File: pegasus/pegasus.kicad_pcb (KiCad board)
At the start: 2 copper layers, 50 x 120 mm, 15 parts, among them IC1 RFD900, IC2 Adafruit_MPL3115A2, IC3 Adafruit-BNO055-PCB, IC4 L70B-M39, IC5 L7805ACV, J1 Conn_01x02_Female, J2 Conn_01x02_Female, U1 Teensy4.1, U2 CON-SMA-EDGE-S, U3 CON-SMA-EDGE-S

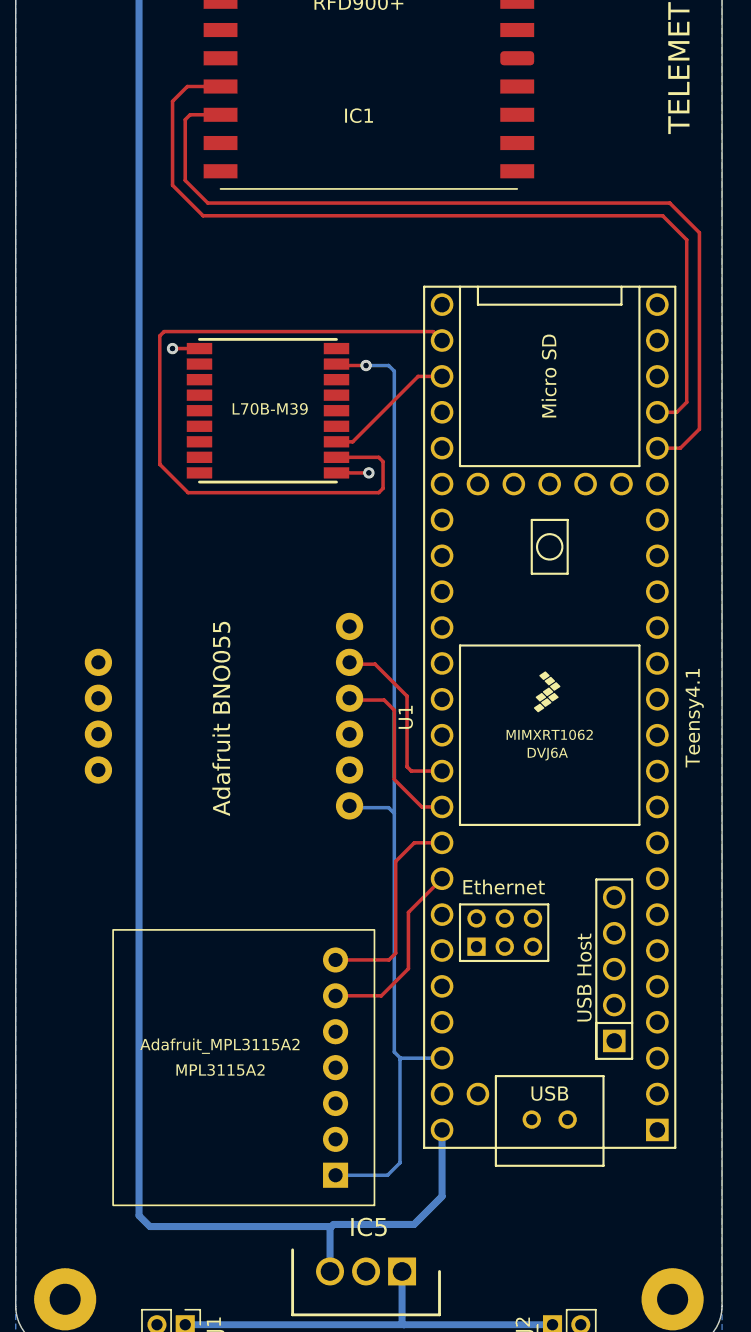
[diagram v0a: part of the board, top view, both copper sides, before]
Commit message: replace teensy 4.1 wih teensy 4, remove barometer and IMU
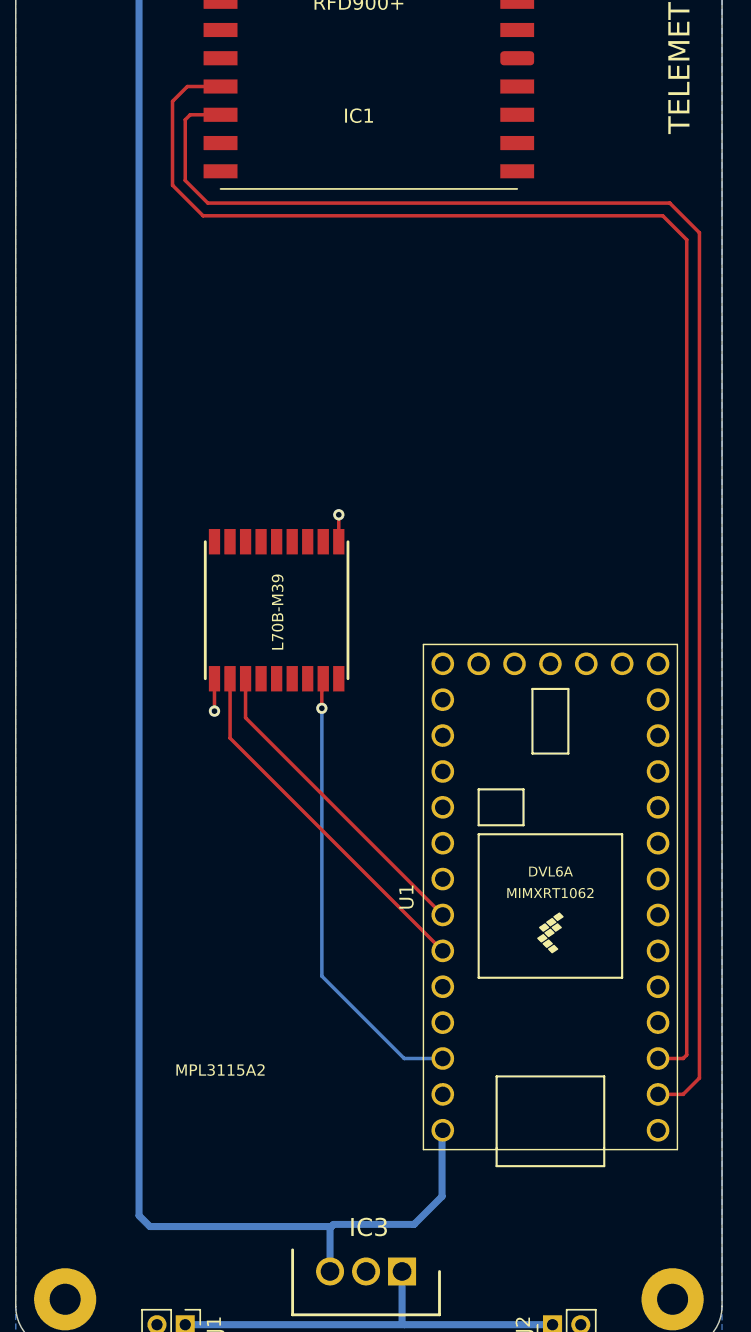
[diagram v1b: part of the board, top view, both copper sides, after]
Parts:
- removed the IC2 at (100.1, 140.1)
- removed the IC3 at (94.6, 115.3)
- IC3: renamed from IC5; footprint Voltage Regulator:TO255P460X1020X2008-3P -> SamaSys:TO255P460X1020X2008-3P
- U1: value Teensy4.1 -> Teensy4.0; footprint Teensy_4.1:Teensy_4.1 -> Teensy:Teensy40
- moved IC2 14.1 mm to (98.5, 107.7), turned to 90 degrees
- moved U1 12.7 mm to (117.8, 128.0)
- renumbered IC4 to IC2
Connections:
- IC2 pad 8: /+3.3V -> 3.3V
- U1 pad 2: unconnected-(U1-Pad2) -> RX7
- U1 pad 20: RX7 -> unconnected-(U1-Pad20)
- U1 pad 21: TX7 -> unconnected-(U1-Pad21)
- U1 pad 26: RX8 -> unconnected-(U1-Pad26)
- U1 pad 28: unconnected-(U1-Pad28) -> RX8
- U1 pad 3: unconnected-(U1-Pad3) -> TX7
- U1 pad 31: unconnected-(U1-Pad31) -> 3.3V
- U1 pad 32: unconnected-(U1-Pad32) -> GND
- U1 pad 33: unconnected-(U1-Pad33) -> +5V
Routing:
- net /+3.3V: track 71.4 -> 0.00 mm, vias 1 -> 0
- net TX7: track 61.6 -> 107.6 mm
- net RX7: track 62.3 -> 108.1 mm
- net 3.3V: track 0.00 -> 32.1 mm, vias 0 -> 1
- net RX8: track 51.5 -> 25.5 mm
- net /SDA: track 14.8 -> 0.00 mm
- net /SCL: track 13.3 -> 0.00 mm
- net TX8: track 9.39 -> 22.5 mm
- net /SCL1: track 12.2 -> 0.00 mm
- net /SDA1: track 12.2 -> 0.00 mm

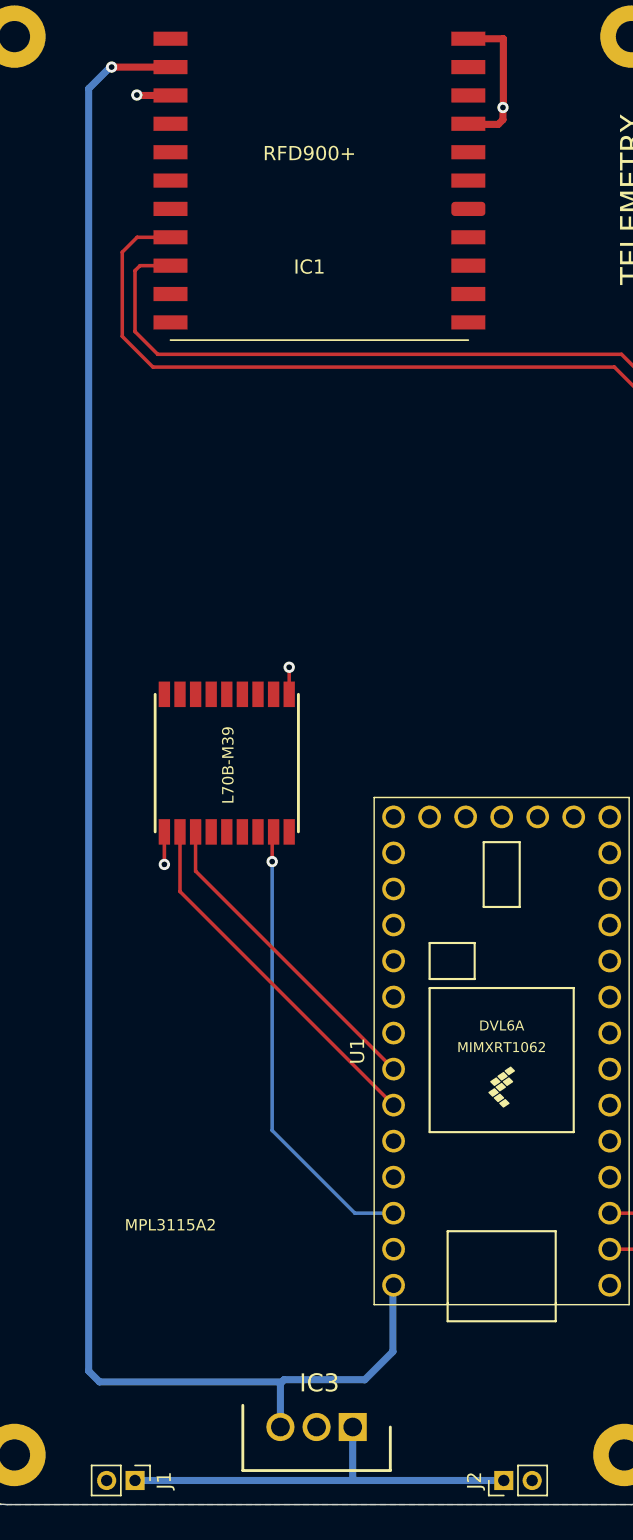
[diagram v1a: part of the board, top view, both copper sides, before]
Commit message: replace sma-connectors with screw terminal with switch
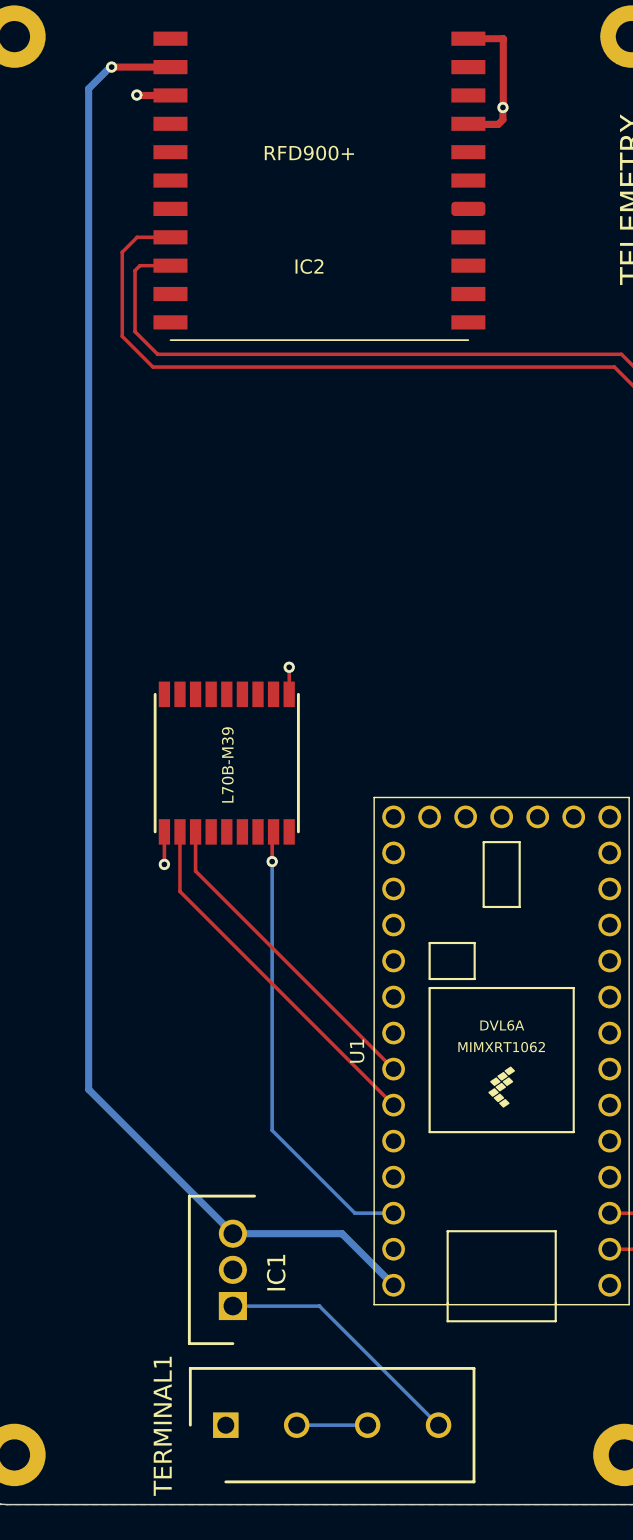
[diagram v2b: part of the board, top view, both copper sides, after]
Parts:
- removed J1, J2: Conn_01x02_Female, Connector_PinHeader_2.00mm:PinHeader_1x02_P2.00mm_Vertical
- added TERMINAL1: Screw_Terminal_01x04, RS-Components:SHDR4W100P0X500_1X4_2000X800X1000P, F.Cu at (98.4, 154.4)
- IC1: renamed from IC3; footprint SamaSys:TO255P460X1020X2008-3P -> RS-Components:TO255P460X1020X2008-3P
- moved IC1 12.0 mm to (98.9, 146.0), turned to 90 degrees
- renumbered IC1 to IC2, IC2 to IC3
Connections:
- IC1 pad 1: +3.7V -> /BATT+
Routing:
- net +3.7V: track 29.8 -> 0.00 mm
- net +5V: track 127.5 -> 104.1 mm
- net /BATT+: track 0.00 -> 18.0 mm
- net Net-(TERMINAL1-Pad2): track 0.00 -> 5.00 mm
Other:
- board text removed: "MPL3115A2"

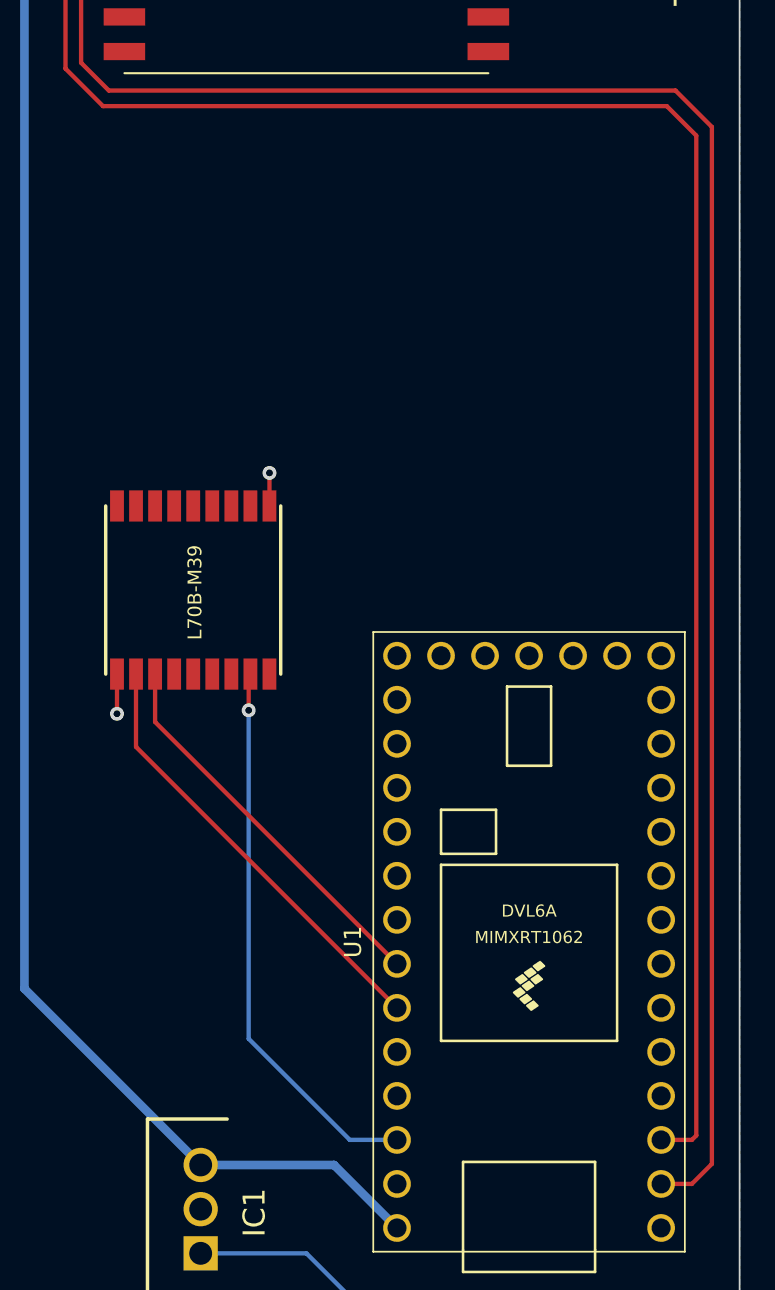
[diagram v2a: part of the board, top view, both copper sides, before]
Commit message: add external RX TX connectors
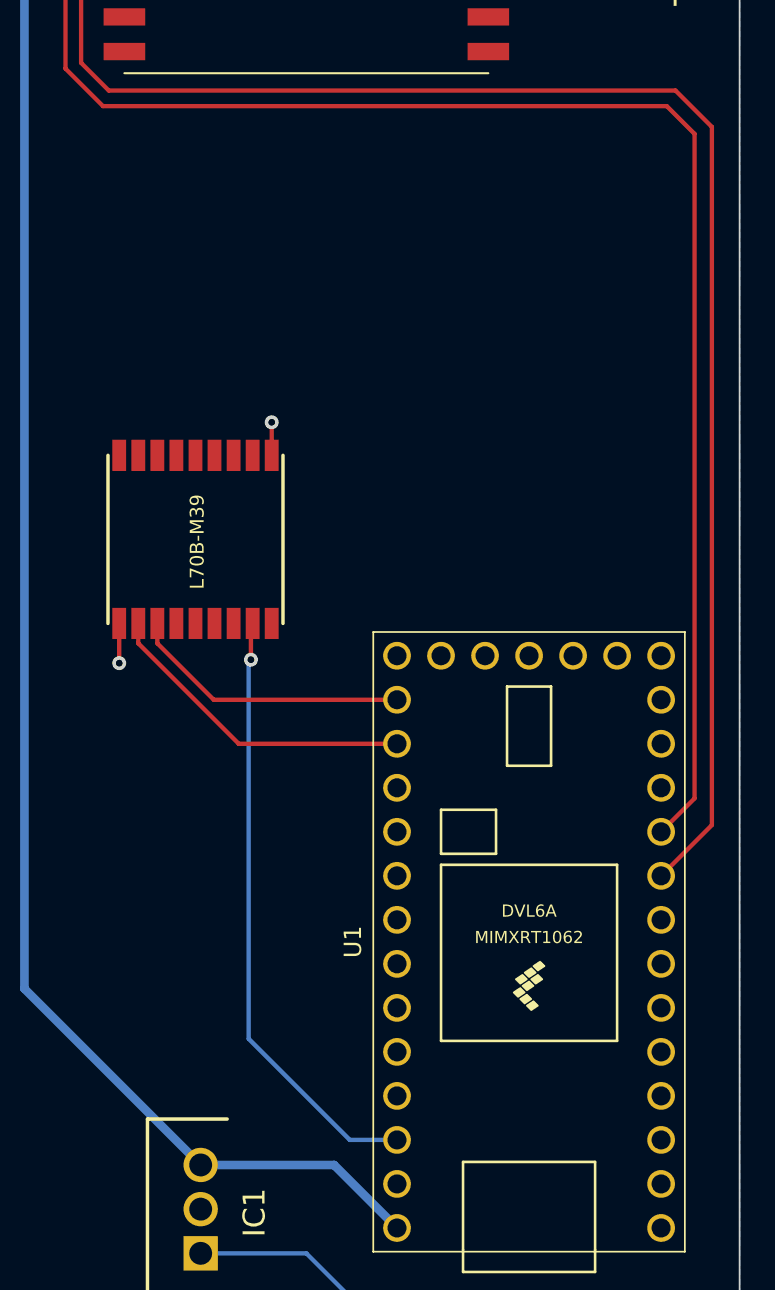
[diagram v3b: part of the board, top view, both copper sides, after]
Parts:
- moved IC3 2.92 mm to (98.6, 104.8)
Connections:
- IC3 pad 2: RX8 -> RX3
- IC3 pad 3: TX8 -> TX3
- U1 pad 10: unconnected-(U1-Pad10) -> TX7
- U1 pad 2: RX7 -> unconnected-(U1-Pad2)
- U1 pad 21: unconnected-(U1-Pad21) -> TX3
- U1 pad 22: unconnected-(U1-Pad22) -> RX3
- U1 pad 27: TX8 -> unconnected-(U1-Pad27)
- U1 pad 28: RX8 -> unconnected-(U1-Pad28)
- U1 pad 3: TX7 -> unconnected-(U1-Pad3)
- U1 pad 9: unconnected-(U1-Pad9) -> RX7
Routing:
- net RX8: track 25.5 -> 0.00 mm
- net TX8: track 22.5 -> 0.00 mm
- net TX7: track 107.6 -> 88.7 mm
- net RX7: track 108.1 -> 89.3 mm
- net RX3: track 0.00 -> 18.5 mm
- net TX3: track 0.00 -> 16.3 mm
- net 3.3V: track 32.1 -> 35.0 mm

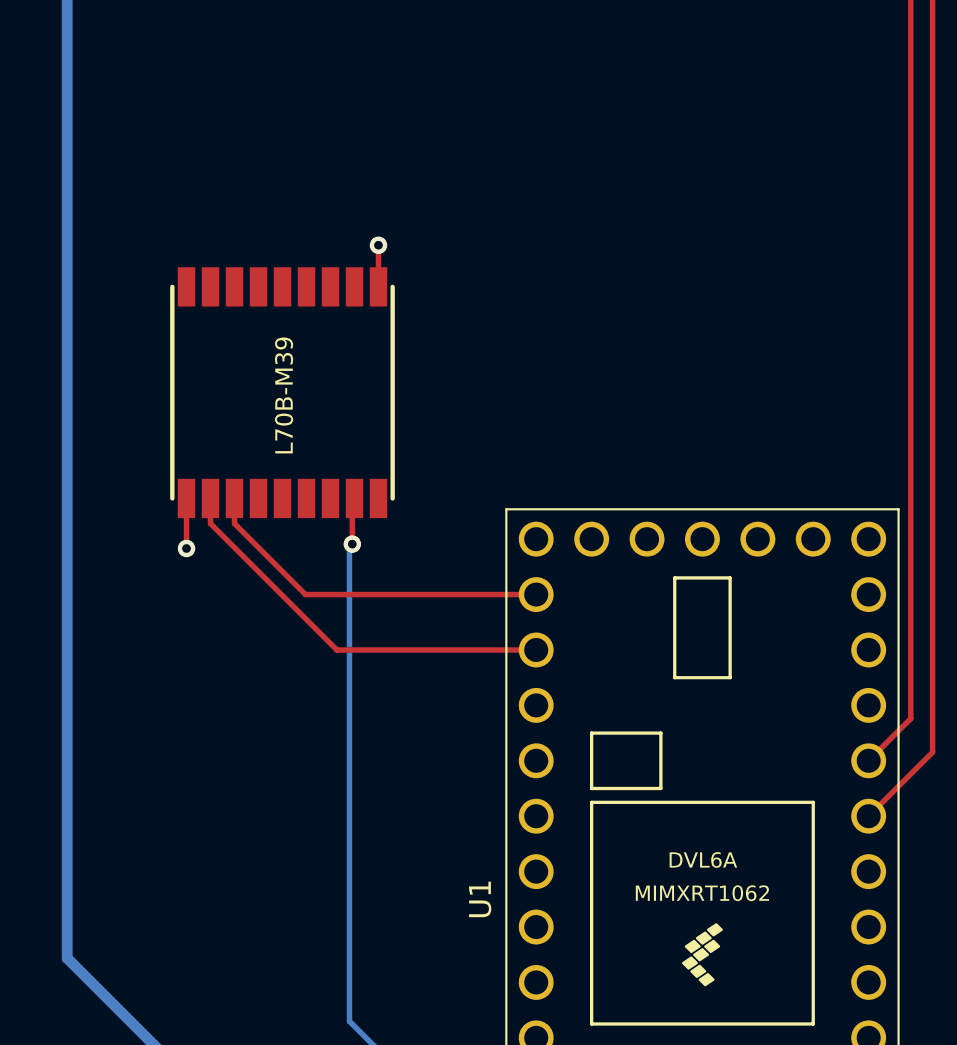
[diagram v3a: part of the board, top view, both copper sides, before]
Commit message: add rgb led
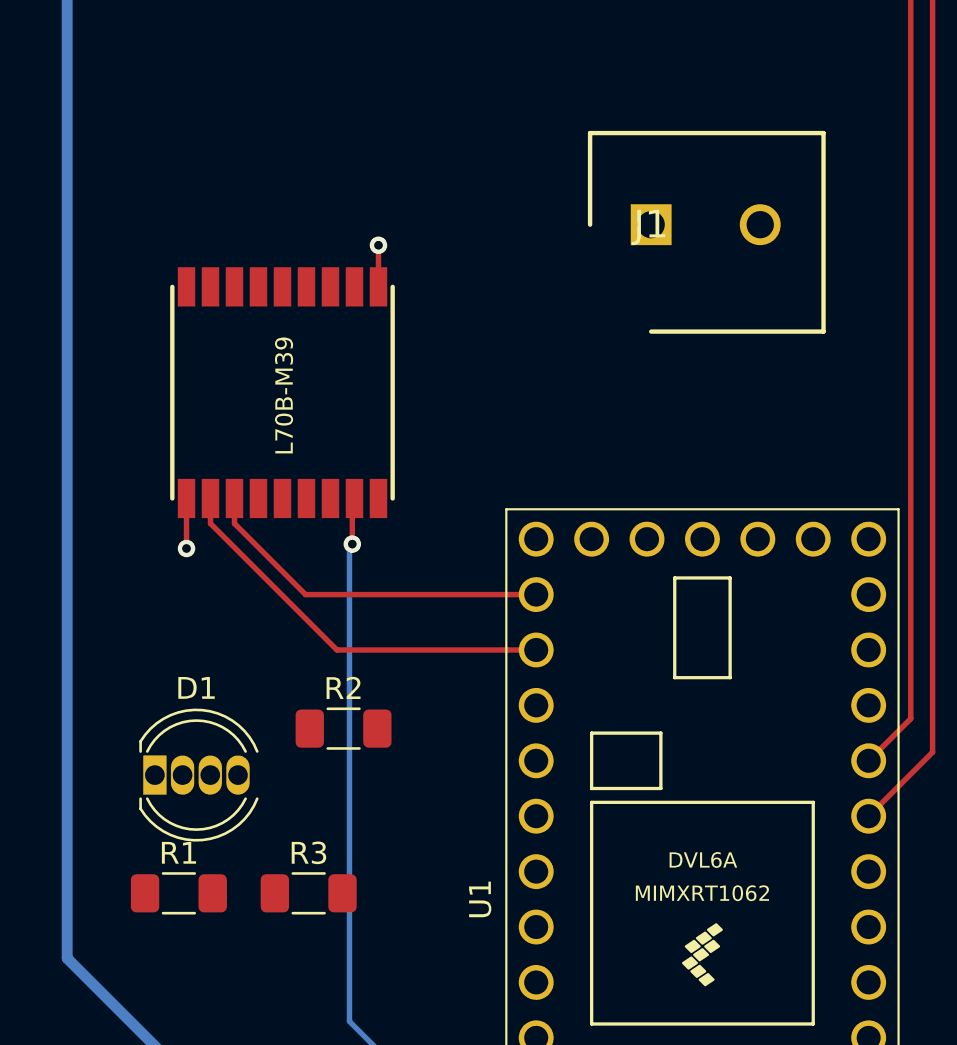
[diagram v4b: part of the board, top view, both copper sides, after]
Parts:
- added D1: RGB LED, LED_THT:LED_D5.0mm-4_RGB, F.Cu at (92.8, 122.3)
- added J1: Screw_Terminal_01x02, RS-Components:SHDR2W105P0X500_1X2_1060X900X1250P, F.Cu at (115.5, 97.1)
- added R1: 220, Resistor_SMD:R_1206_3216Metric_Pad1.30x1.75mm_HandSolder, F.Cu at (93.8, 127.8)
- added R2: 220, Resistor_SMD:R_1206_3216Metric_Pad1.30x1.75mm_HandSolder, F.Cu at (101.4, 120.2)
- added R3: 220, Resistor_SMD:R_1206_3216Metric_Pad1.30x1.75mm_HandSolder, F.Cu at (99.8, 127.8)
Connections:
- U1 pad 23: unconnected-(U1-Pad23) -> RGB1
- U1 pad 24: unconnected-(U1-Pad24) -> RGB2
- U1 pad 25: unconnected-(U1-Pad25) -> RGB3
